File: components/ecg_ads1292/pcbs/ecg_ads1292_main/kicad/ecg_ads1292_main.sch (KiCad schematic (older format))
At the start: 16 parts, among them J1 Conn_02x04_Odd_Even, P1 Conn_02x20_Odd_Even

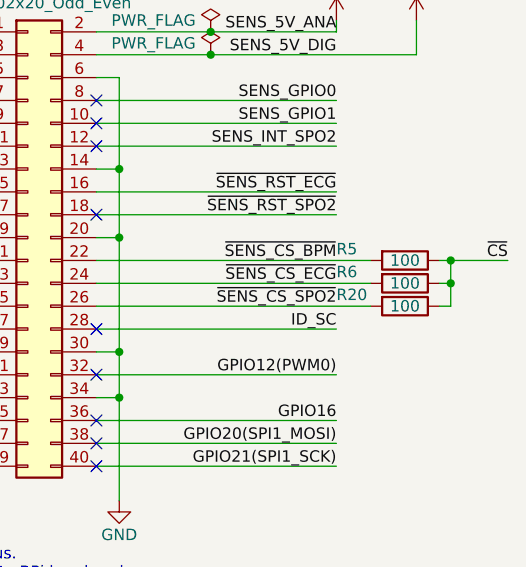
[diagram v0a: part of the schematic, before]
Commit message: update parts and add digikey PNs
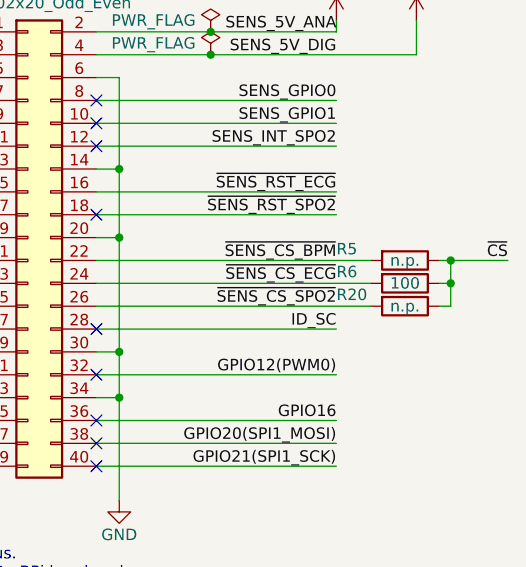
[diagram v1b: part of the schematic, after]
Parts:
- J1: MPN (none) -> TSW-104-08-T-D-RA; Manufacturer (none) -> SAMTEC; PN Digi-Key (none) -> SAM1049-04-ND
- P1: MPN (none) -> 4P01-2D02-DA; Manufacturer (none) -> 3M; PN Digi-Key (none) -> 3M10620-ND; PN Farnell (none) -> 2672560
- R20: value 100 -> n.p.; PN Farnell 1739145 -> (none)
- R5: value 100 -> n.p.; MPN (none) -> CRCW0603100RJNEA; Manufacturer (none) -> VISHAY; PN Digi-Key (none) -> 541-100GCT-ND; PN Farnell 1739145 -> 2616742
- R6: MPN (none) -> CRCW0603100RJNEA; Manufacturer (none) -> VISHAY; PN Digi-Key (none) -> 541-100GCT-ND; PN Farnell 1739145 -> 2616742
- R7, R8: MPN (none) -> CRCW0603100KJNEA; Manufacturer (none) -> VISHAY; PN Digi-Key (none) -> 541-100KGCT-ND; PN Farnell 1738916 -> 1692517

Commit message: archive all components
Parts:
- J1: symbol Connector_Generic:Conn_02x04_Odd_Even -> ecg_ads1292_main:Conn_02x04_Odd_Even
- MK1, MK2, MK3, MK4: symbol Mechanical:MountingHole -> ecg_ads1292_main:MountingHole
- P1: symbol Connector_Generic:Conn_02x20_Odd_Even -> ecg_ads1292_main:Conn_02x20_Odd_Even
- TP15, TP5: symbol Connector:TestPoint_Flag -> ecg_ads1292_main:TestPoint_Flag
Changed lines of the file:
@@
 $EndSheet
 $Comp
-L power:+5VA #PWR012
+L ecg_ads1292_main:+5VA #PWR012
 U 1 1 580C1B61
 P 15200 2400
@@
 $EndComp
 $Comp
-L power:GND #PWR011
+L ecg_ads1292_main:GND #PWR011
 U 1 1 580C1D11
 P 14250 4500
@@
 $EndComp
 $Comp
-L power:GND #PWR010
+L ecg_ads1292_main:GND #PWR010
 U 1 1 580C1E01
 P 13550 4500
@@
 $EndComp
 $Comp
-L power:+3.3VA #PWR09
+L ecg_ads1292_main:+3.3VA #PWR09
 U 1 1 580C1BC1
 P 12500 2400
@@
 $EndComp
 $Comp
-L Mechanical:MountingHole MK1
+L ecg_ads1292_main:MountingHole MK1
 U 1 1 5834FB2E
 P 13400 8100
@@
 $EndComp
 $Comp
-L Mechanical:MountingHole MK3
+L ecg_ads1292_main:MountingHole MK3
 U 1 1 5834FBEF
 P 13950 8100
@@
 $EndComp
 $Comp
-L Mechanical:MountingHole MK2
+L ecg_ads1292_main:MountingHole MK2
 U 1 1 5834FC19
 P 13400 8350
@@
 $EndComp
 $Comp
-L Mechanical:MountingHole MK4
+L ecg_ads1292_main:MountingHole MK4
 U 1 1 5834FC4F
 P 13950 8350
@@
 $EndComp
 $Comp
-L power:+5VD #PWR013
+L ecg_ads1292_main:+5VD #PWR013
 U 1 1 5EA6E5C1
 P 15550 2400
@@
 $EndComp
 $Comp
-L power:+3.3V #PWR08
+L ecg_ads1292_main:+3.3V #PWR08
 U 1 1 5EA72FFE
 P 12150 2400
@@
 $EndComp
 $Comp
-L Connector:TestPoint_Flag TP15
+L ecg_ads1292_main:TestPoint_Flag TP15
 U 1 1 5EB284C8
 P 7450 7050
@@
 $EndComp
 $Comp
-L Connector:TestPoint_Flag TP5
+L ecg_ads1292_main:TestPoint_Flag TP5
 U 1 1 5EB28150
 P 4500 6600
@@
 $EndComp
 $Comp
-L power:+5VA #PWR05
+L ecg_ads1292_main:+5VA #PWR05
 U 1 1 5EB064ED
 P 8200 5550
@@
 $EndComp
 $Comp
-L power:+3.3V #PWR06
+L ecg_ads1292_main:+3.3V #PWR06
 U 1 1 5EB0751F
 P 8400 4550
@@
 $EndComp
 $Comp
-L Connector_Generic:Conn_02x04_Odd_Even J1
+L ecg_ads1292_main:Conn_02x04_Odd_Even J1
 U 1 1 5EB3B000
 P 4000 5300
@@
 $EndComp
 $Comp
-L power:PWR_FLAG #FLG01
+L ecg_ads1292_main:PWR_FLAG #FLG01
 U 1 1 5E91687C
 P 3500 6150
@@
 $EndComp
 $Comp
-L power:GNDPWR #PWR01
+L ecg_ads1292_main:GNDPWR #PWR01
 U 1 1 5E898834
 P 3650 6750
@@
 $EndComp
 $Comp
-L power:PWR_FLAG #FLG0101
+L ecg_ads1292_main:PWR_FLAG #FLG0101
 U 1 1 5EAAEF5C
 P 14650 2450
@@
 $EndComp
 $Comp
-L power:PWR_FLAG #FLG0102
+L ecg_ads1292_main:PWR_FLAG #FLG0102
 U 1 1 5EAAFB53
 P 14650 2550
@@
 $EndComp
 $Comp
-L power:PWR_FLAG #FLG0103
+L ecg_ads1292_main:PWR_FLAG #FLG0103
 U 1 1 5EAAFE25
 P 13150 2450
@@
 $EndComp
 $Comp
-L power:PWR_FLAG #FLG0104
+L ecg_ads1292_main:PWR_FLAG #FLG0104
 U 1 1 5EAB0869
 P 13100 3250
@@
 $EndComp
 $Comp
-L power:PWR_FLAG #FLG0105
+L ecg_ads1292_main:PWR_FLAG #FLG0105
 U 1 1 5EB05147
 P 13500 4350
@@
 $EndComp
 $Comp
-L Connector_Generic:Conn_02x20_Odd_Even P1
+L ecg_ads1292_main:Conn_02x20_Odd_Even P1
 U 1 1 59AD464A
 P 13850 3350
